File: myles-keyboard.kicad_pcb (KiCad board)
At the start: 2 copper layers, 208.8 x 114.3 mm, 56 parts, among them J1 TRRS, J2 OLED, SW01 Key, SW02 Key, SW03 Key, SW04 Key, SW11 Key, SW12 Key, SW13 Key, SW14 Key, SW15 Key, SW16 Key, SW17 Key, SW18 Key, SW19 Key, SW21 Key, SW22 Key, SW23 Key, SW24 Key, SW25 Key, SW26 Key, SW27 Key, SW28 Key, SW29 Key, SW30 Key, SW31 Key, SW32 Key, SW33 Key, SW34 Key, SW35 Key, SW36 Key, SW37 Key, SW38 Key, SW39 Key, SW40 Key, SW41 Key, SW42 Key, SW43 Key, SW44 Key, SW45 Key, SW46 Key, SW47 Key, SW48 Key, SW49 Key, U1 ProMicro

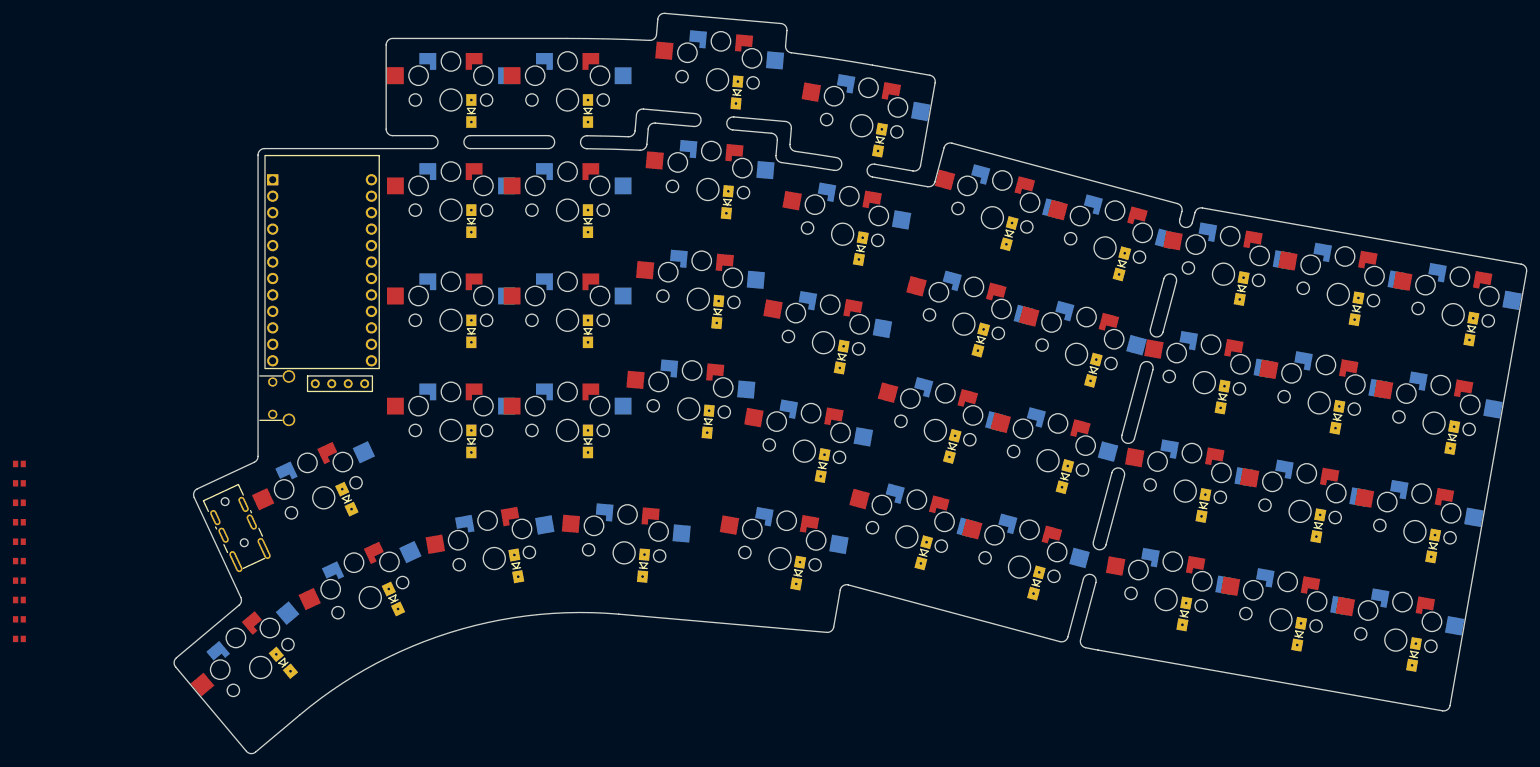
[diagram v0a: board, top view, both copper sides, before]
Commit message: add 3d model for plate for main pcb
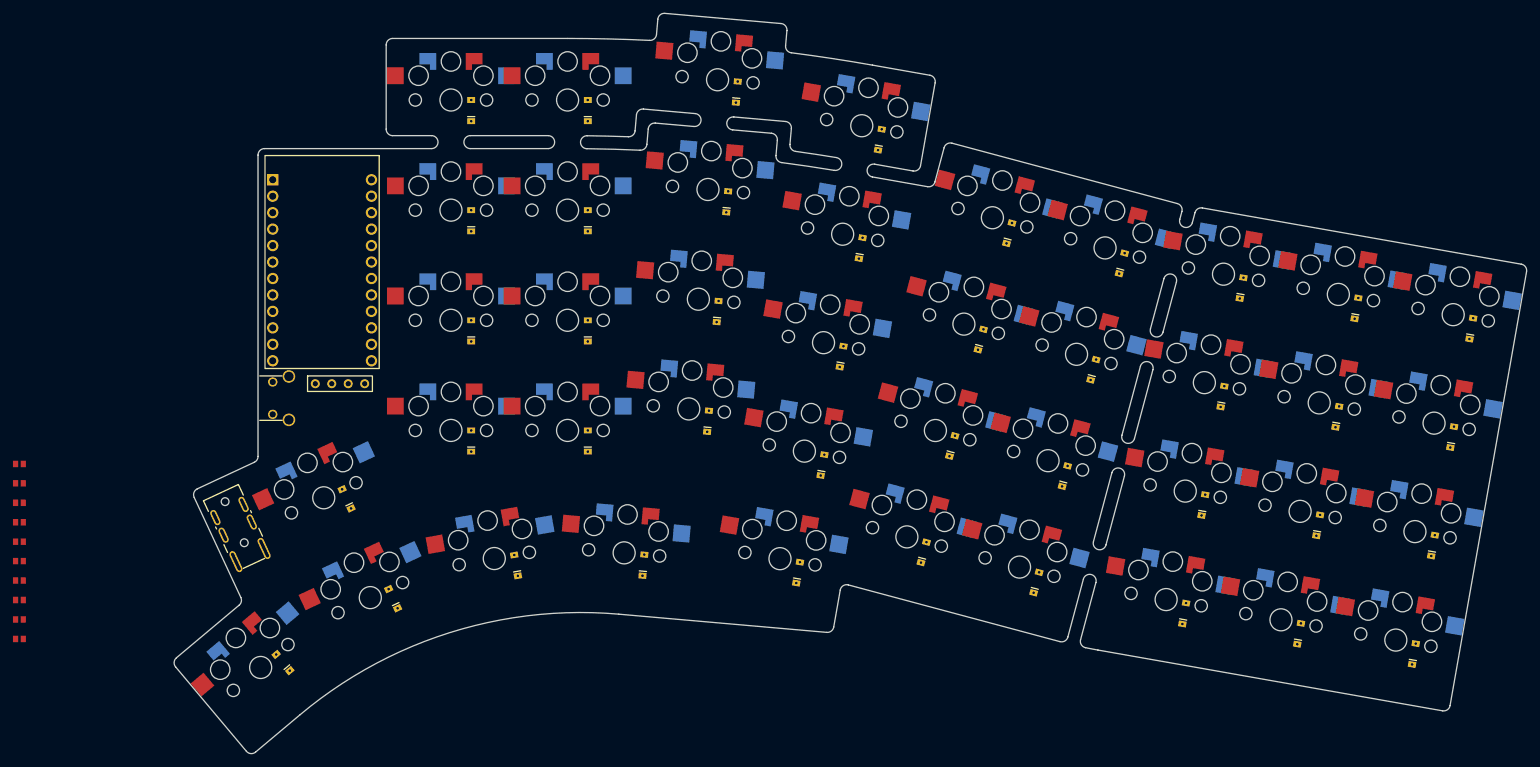
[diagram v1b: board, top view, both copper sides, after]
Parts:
- added REF**: RightPlate, myles-keyboard:RightPlate, F.Cu at (0.00, 0.00)

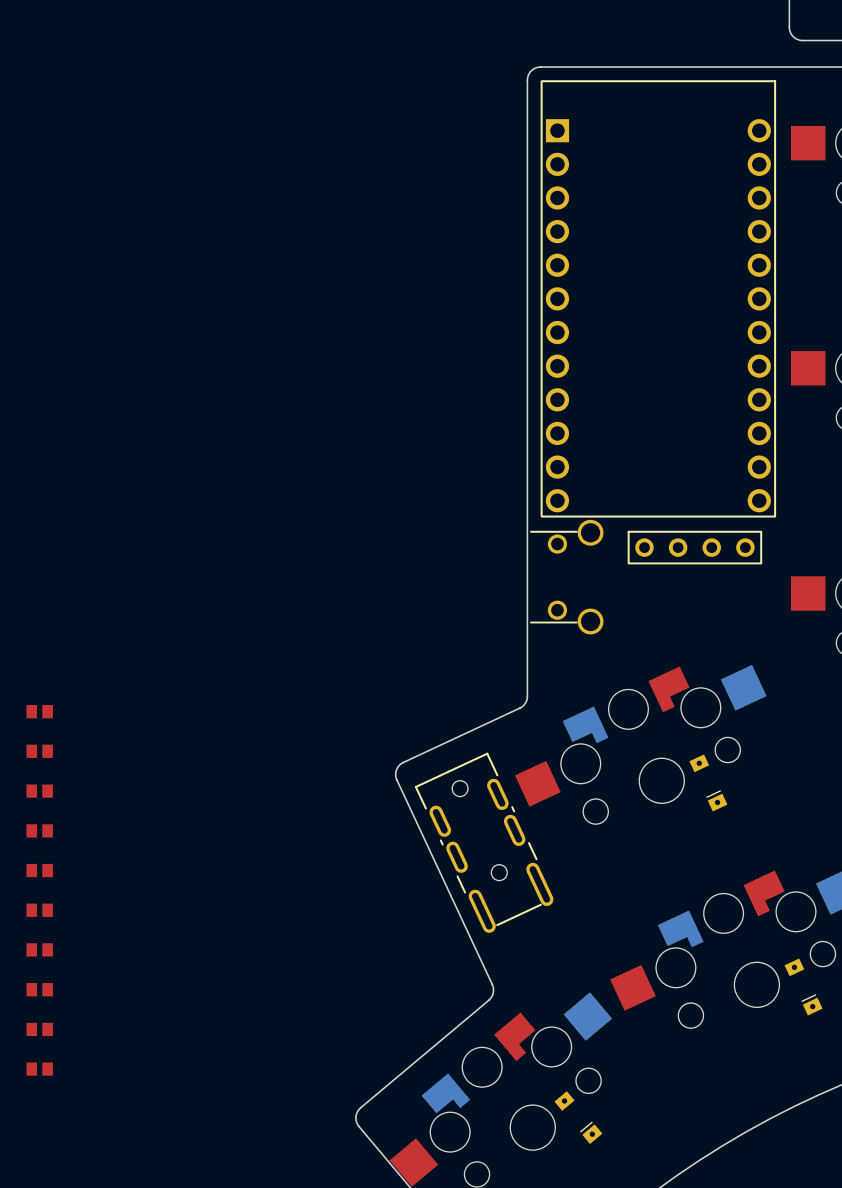
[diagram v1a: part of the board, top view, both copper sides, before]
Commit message: rearrange TRRS jack
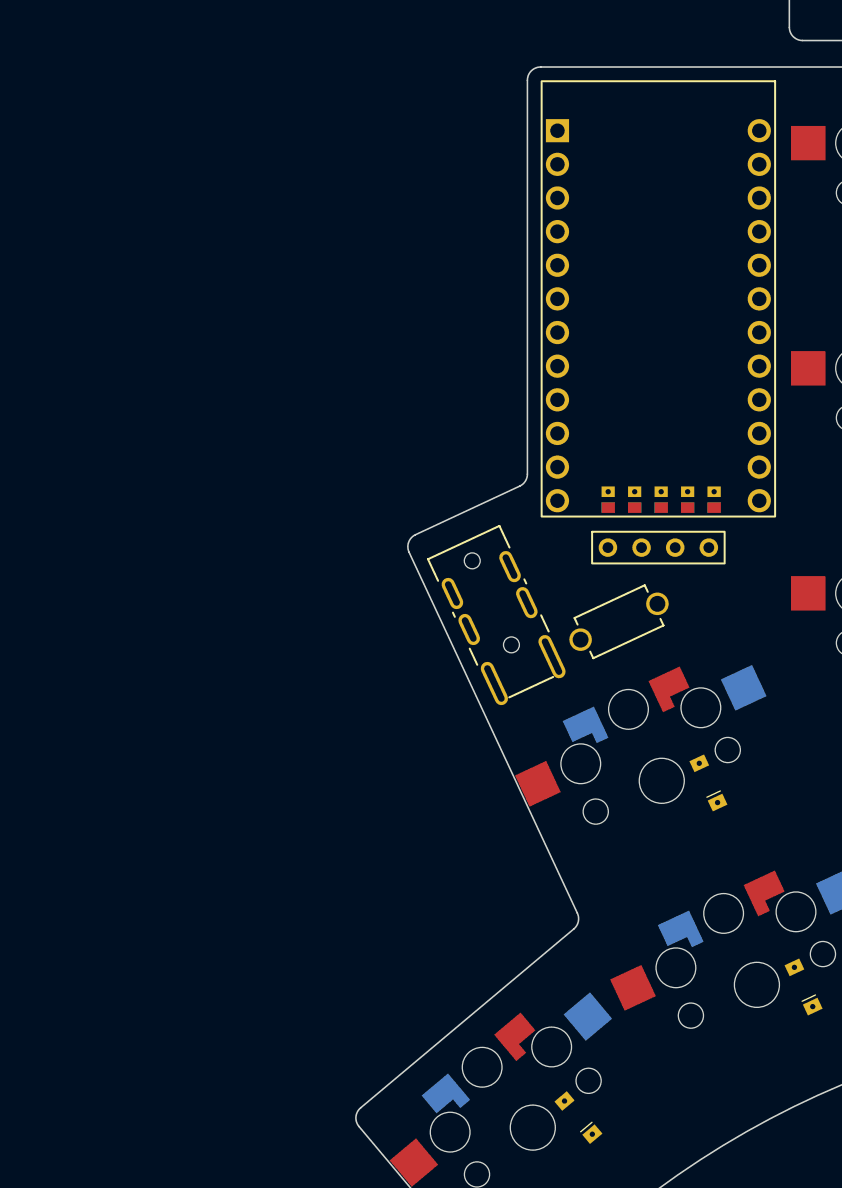
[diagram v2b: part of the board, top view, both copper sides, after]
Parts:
- removed JP10, JP6, JP7, JP8, JP9: Jumper_2_Open, myles-keyboard:Jumper
- removed REF**: RightPlate, myles-keyboard:RightPlate
- added H1: ~, myles-keyboard:RightPlate, F.Cu at (0.00, 0.00)
- JP1, JP2, JP3, JP4, JP5: value Jumper_2_Open -> ~
- SW_RST1: footprint myles-keyboard:MJTP1117 -> myles-keyboard:PTS636
- moved JP5 58.1 mm to (64.1, 82.7), turned to -90 degrees
- moved JP4 54.9 mm to (62.1, 82.7), turned to -90 degrees
- moved JP3 51.8 mm to (60.1, 82.7), turned to -90 degrees
- moved JP2 48.8 mm to (58.1, 82.7), turned to -90 degrees
- moved JP1 45.8 mm to (56.1, 82.7), turned to -90 degrees
- moved J1 17.2 mm to (47.3, 90.5)
- moved SW_RST1 5.78 mm to (56.9, 91.9), turned to 25 degrees
- moved J2 2.76 mm to (59.9, 86.3)
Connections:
- J1 pad 3: Net-(JP1-A) -> Net-(J1-Pad3)
- J1 pad 4: Net-(JP2-B) -> Net-(J1-Pad4)
- J2 pad 1: Net-(JP3-B) -> Net-(J2-Pad1)
- J2 pad 2: Net-(JP4-B) -> Net-(J2-Pad2)
- J2 pad 3: Net-(JP5-B) -> Net-(J2-Pad3)
- J2 pad 4: Net-(JP10-B) -> Net-(J2-Pad4)
- JP1 pad 1: Net-(JP1-A) -> VCC
- JP1 pad 2: VCC -> Net-(J1-Pad3)
- JP2 pad 1: VCC -> Net-(J2-Pad1)
- JP2 pad 2: Net-(JP2-B) -> SDA
- JP3 pad 1: GND -> Net-(J2-Pad2)
- JP3 pad 2: Net-(JP3-B) -> SCL
- JP4 pad 1: VCC -> Net-(J2-Pad3)
- JP4 pad 2: Net-(JP4-B) -> VCC
- JP5 pad 1: SCL -> Net-(J2-Pad4)
- JP5 pad 2: Net-(JP5-B) -> GND
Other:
- outline, holes or cut-outs redrawn

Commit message: reorder jumpers
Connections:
- JP2 pad 1: Net-(J2-Pad1) -> GND
- JP2 pad 2: SDA -> Net-(J2-Pad4)
- JP2 pad 3: GND -> Net-(J2-Pad1)
- JP3 pad 1: Net-(J2-Pad2) -> VCC
- JP3 pad 2: SCL -> Net-(J2-Pad3)
- JP3 pad 3: VCC -> Net-(J2-Pad2)
- JP4 pad 1: Net-(J2-Pad3) -> SCL
- JP4 pad 2: VCC -> Net-(J2-Pad2)
- JP4 pad 3: SCL -> Net-(J2-Pad3)
- JP5 pad 1: Net-(J2-Pad4) -> SDA
- JP5 pad 2: GND -> Net-(J2-Pad1)
- JP5 pad 3: SDA -> Net-(J2-Pad4)

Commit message: start adding traces
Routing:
- net col1: track 0.00 -> 190.4 mm, vias 0 -> 2
- net row1: track 0.00 -> 165.8 mm
- net row4: track 0.00 -> 162.6 mm
- net row3: track 0.00 -> 158.7 mm
- net row2: track 0.00 -> 140.8 mm
- net col3: track 0.00 -> 87.6 mm, vias 0 -> 2
- net col2: track 0.00 -> 86.3 mm
- net col8: track 0.00 -> 68.8 mm, vias 0 -> 4
- net row0: track 0.00 -> 67.0 mm
- net col7: track 0.00 -> 62.9 mm, vias 0 -> 2
- net col4: track 0.00 -> 60.8 mm, vias 0 -> 1
- net col6: track 0.00 -> 58.7 mm, vias 0 -> 1
- net col5: track 0.00 -> 58.3 mm, vias 0 -> 1
- net col0: track 0.00 -> 35.6 mm
- net Net-(SW18-Pad3): track 0.00 -> 11.9 mm, vias 0 -> 1
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
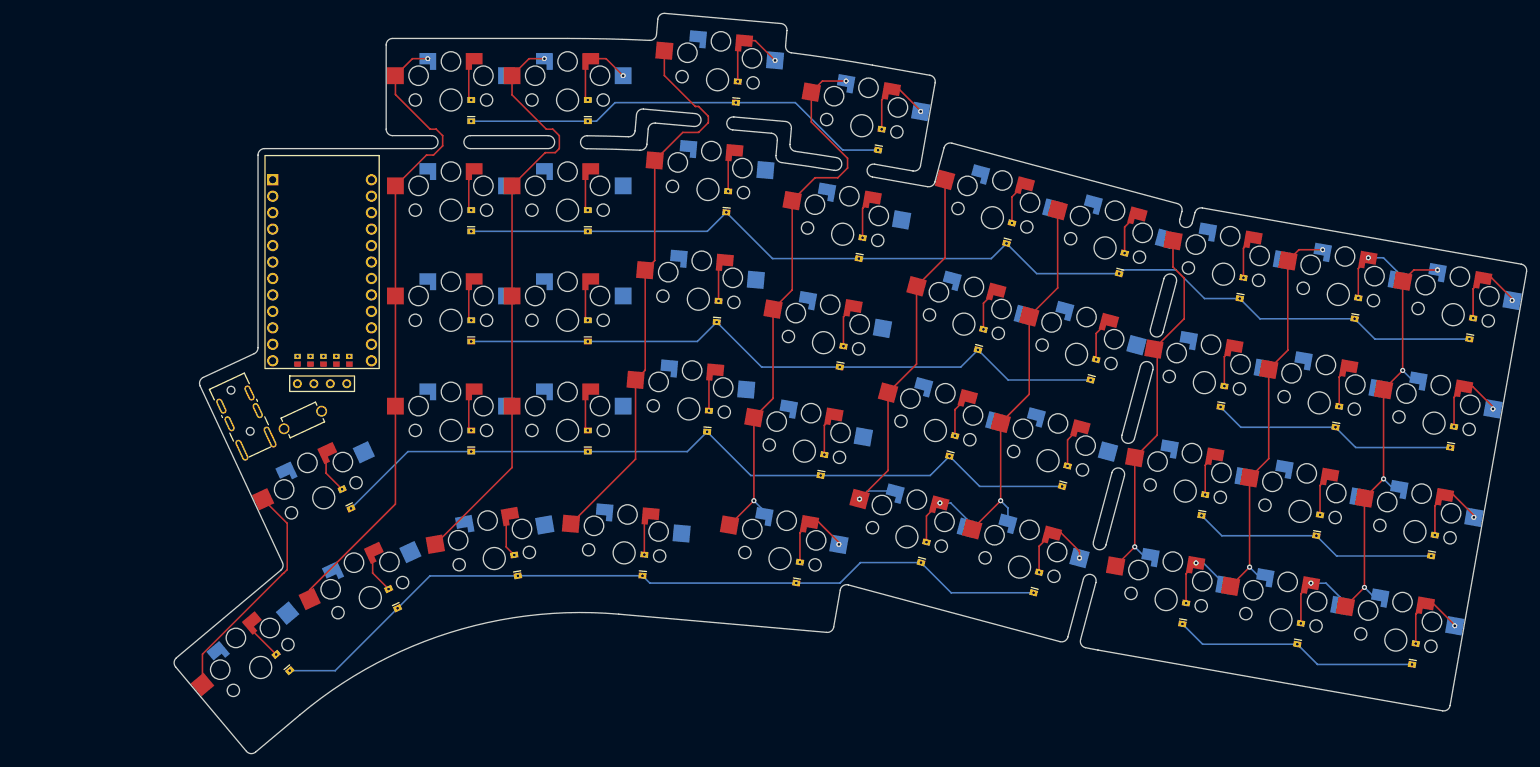
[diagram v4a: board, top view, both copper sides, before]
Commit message: add lots of traces
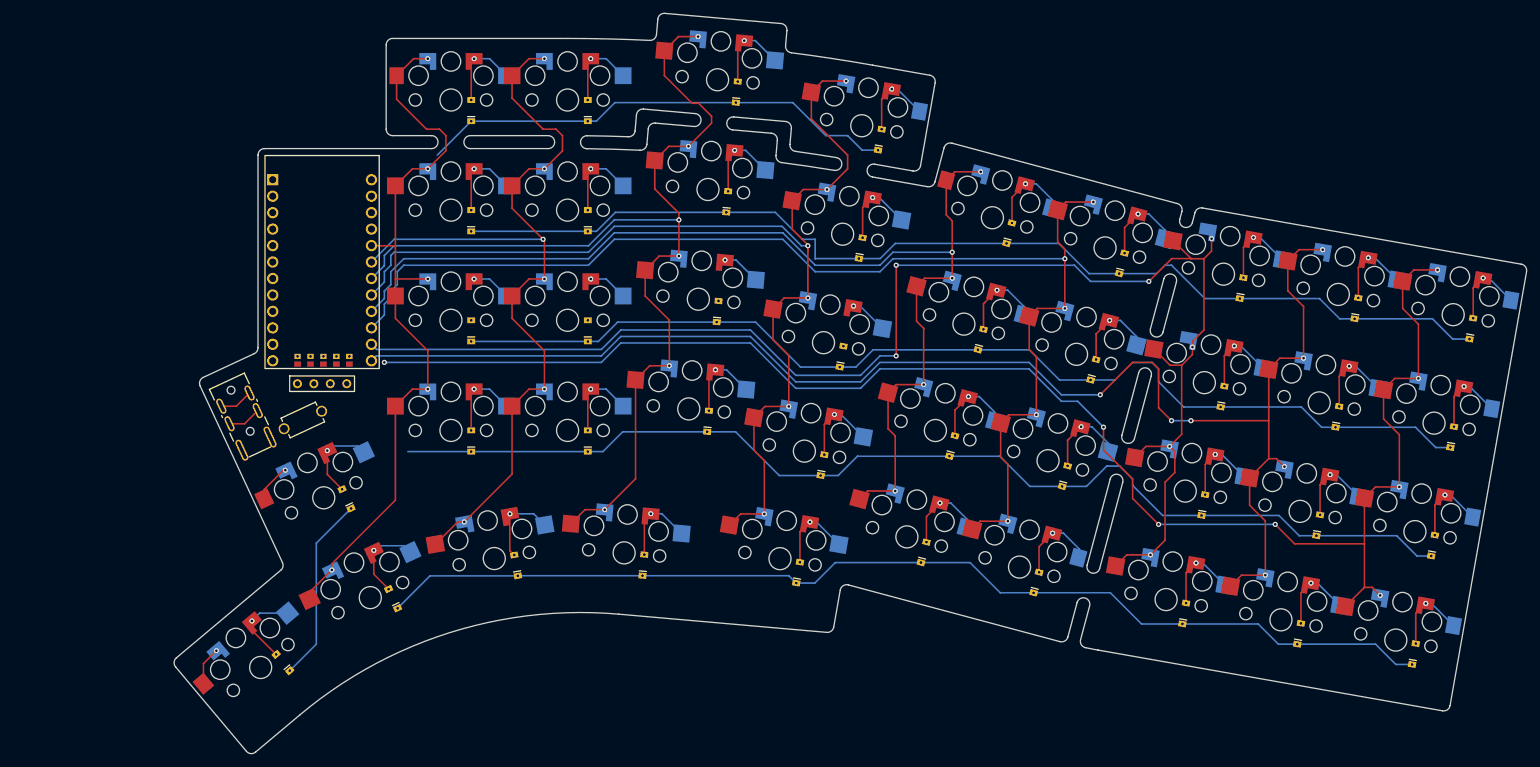
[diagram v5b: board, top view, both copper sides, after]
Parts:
- SW00: renamed from SW01; footprint myles-keyboard:Key -> myles-keyboard:KeyLeft
- SW03: renamed from SW04; footprint myles-keyboard:Key -> myles-keyboard:KeyRight
- SW04: renamed from SW40; footprint myles-keyboard:Key -> myles-keyboard:KeyLeft
- SW05: renamed from SW30; footprint myles-keyboard:Key -> myles-keyboard:KeyLeft
- SW14: renamed from SW15; footprint myles-keyboard:Key -> myles-keyboard:KeyLeft
- SW18: renamed from SW19; footprint myles-keyboard:Key -> myles-keyboard:KeyRight
- SW28: renamed from SW29; footprint myles-keyboard:Key -> myles-keyboard:KeyRight
- SW38: renamed from SW39; footprint myles-keyboard:Key -> myles-keyboard:KeyRight
- SW45: renamed from SW46; footprint myles-keyboard:Key -> myles-keyboard:KeyRight
- SW48: renamed from SW49; footprint myles-keyboard:Key -> myles-keyboard:KeyRight
- renumbered SW02 to SW01, SW03 to SW02, SW11 to SW10, SW12 to SW11, SW13 to SW12, SW14 to SW13, SW16 to SW15, SW17 to SW16, SW18 to SW17, SW21 to SW20, SW22 to SW21, SW23 to SW22, SW24 to SW23, SW25 to SW24, SW26 to SW25, SW27 to SW26, SW28 to SW27, SW31 to SW30, SW32 to SW31, SW33 to SW32, SW34 to SW33, SW35 to SW34, SW36 to SW35, SW37 to SW36, SW38 to SW37, SW41 to SW40, SW42 to SW41, SW43 to SW42, SW44 to SW43, SW45 to SW44, SW47 to SW46, SW48 to SW47
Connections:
- SW00 pad 1: col1 -> col0
- SW00 pad 2: col1 -> col0
- SW04 pad 1: col0 -> col4
- SW04 pad 2: col0 -> col4
- SW04 pad 6: row4 -> row0
- SW05 pad 1: col0 -> col5
- SW05 pad 2: col0 -> col5
- SW05 pad 6: row3 -> row0
- SW10 pad 1: col1 -> col0
- SW10 pad 2: col1 -> col0
- SW20 pad 1: col1 -> col0
- SW20 pad 2: col1 -> col0
- SW30 pad 1: col1 -> col0
- SW30 pad 2: col1 -> col0
- SW40 pad 1: col1 -> col0
- SW40 pad 2: col1 -> col0
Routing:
- net col8: track 68.8 -> 242.9 mm, vias 4 -> 8
- net col6: track 58.7 -> 225.8 mm, vias 1 -> 7
- net col7: track 62.9 -> 226.8 mm, vias 2 -> 7
- net col5: track 58.3 -> 195.3 mm, vias 1 -> 6
- net col4: track 60.8 -> 176.1 mm, vias 1 -> 6
- net col3: track 87.6 -> 172.4 mm, vias 2 -> 6
- net col0: track 35.6 -> 115.3 mm, vias 0 -> 5
- net col2: track 86.3 -> 157.1 mm, vias 0 -> 6
- net col1: track 190.4 -> 132.0 mm, vias 2 -> 6
- net row0: track 67.0 -> 103.4 mm
- net row2: track 140.8 -> 166.0 mm
- net row3: track 158.7 -> 172.8 mm
- net Net-(SW34-Pad3): track 5.39 -> 13.4 mm, vias 0 -> 1
- net Net-(SW14-Pad3): track 5.39 -> 13.4 mm, vias 0 -> 1
- net Net-(SW15-Pad3): track 5.39 -> 13.4 mm, vias 0 -> 1
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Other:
- outline, holes or cut-outs redrawn

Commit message: setup wiring around promicro
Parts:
- moved JP1 9.25 mm to (56.9, 91.9), turned to -155 degrees
- moved JP5 7.89 mm to (62.7, 74.9)
- moved JP2 7.82 mm to (57.1, 74.9)
- moved JP3 5.18 mm to (58.6, 77.7)
- moved JP4 5.05 mm to (61.2, 77.7)
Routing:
- net col4: track 176.1 -> 242.6 mm
- net DATA: track 5.19 -> 62.9 mm, vias 0 -> 1
- net VCC: track 0.00 -> 50.0 mm, vias 0 -> 1
- net RESET: track 0.00 -> 43.7 mm
- net col5: track 195.3 -> 228.5 mm
- net GND: track 5.19 -> 33.3 mm, vias 0 -> 1
- net col8: track 242.9 -> 267.7 mm, vias 8 -> 9
- net SCL: track 0.00 -> 23.7 mm, vias 0 -> 1
- net SDA: track 0.00 -> 19.8 mm, vias 0 -> 1
- net Net-(J2-Pad4): track 0.00 -> 17.4 mm, vias 0 -> 1
- net Net-(J2-Pad1): track 0.00 -> 17.4 mm, vias 0 -> 1
- net Net-(J2-Pad2): track 0.00 -> 11.2 mm, vias 0 -> 1
- net Net-(J2-Pad3): track 0.00 -> 11.2 mm, vias 0 -> 1
- net Net-(SW23-Pad3): track 5.90 -> 12.7 mm
- net Net-(SW22-Pad3): track 6.02 -> 12.7 mm
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
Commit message: draft wiring
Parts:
- SW10, SW20: footprint myles-keyboard:Key -> myles-keyboard:KeyLeft
- moved JP2 3.46 mm to (58.6, 78.0)
- moved JP5 3.46 mm to (61.2, 78.0)
- moved JP3 3.11 mm to (58.6, 80.8)
- moved JP4 3.11 mm to (61.2, 80.8)
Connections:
- U1 pad 10: row3 -> col3
- U1 pad 11: row4 -> col4
- U1 pad 12: col8 -> col5
- U1 pad 13: col7 -> row4
- U1 pad 14: col6 -> row3
- U1 pad 15: col5 -> col8
- U1 pad 16: col4 -> col7
- U1 pad 17: col3 -> col6
- U1 pad 18: col2 -> row2
- U1 pad 19: col1 -> col0
- U1 pad 20: col0 -> row0
- U1 pad 7: row0 -> row1
- U1 pad 8: row1 -> col1
- U1 pad 9: row2 -> col2
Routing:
- net row0: track 103.4 -> 169.5 mm, vias 0 -> 1
- net row1: track 168.2 -> 216.5 mm
- net GND: track 33.3 -> 75.0 mm
- net row4: track 167.0 -> 203.9 mm
- net col1: track 131.9 -> 161.9 mm
- net col4: track 242.6 -> 271.3 mm
- net col2: track 156.2 -> 184.9 mm
- net DATA: track 62.9 -> 37.1 mm, vias 1 -> 0
- net col3: track 178.9 -> 203.8 mm
- net row2: track 166.0 -> 186.3 mm
- net row3: track 172.8 -> 191.7 mm
- net VCC: track 50.0 -> 66.2 mm, vias 1 -> 2
- net col5: track 228.5 -> 243.6 mm
- net col8: track 267.7 -> 256.1 mm, vias 9 -> 7
- net Net-(J1-Pad3): track 0.00 -> 11.2 mm
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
